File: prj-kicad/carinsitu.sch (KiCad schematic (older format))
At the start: 37 parts, among them P1 BAT, P2 MOT, P3 CONN_3, P4 CONN_1, SW1 SWITCH_SLIDE, U1 ESP32, U2 MIC2860, U3 STC3100, U4 SN74LVC1T45, U7 LSM6D3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

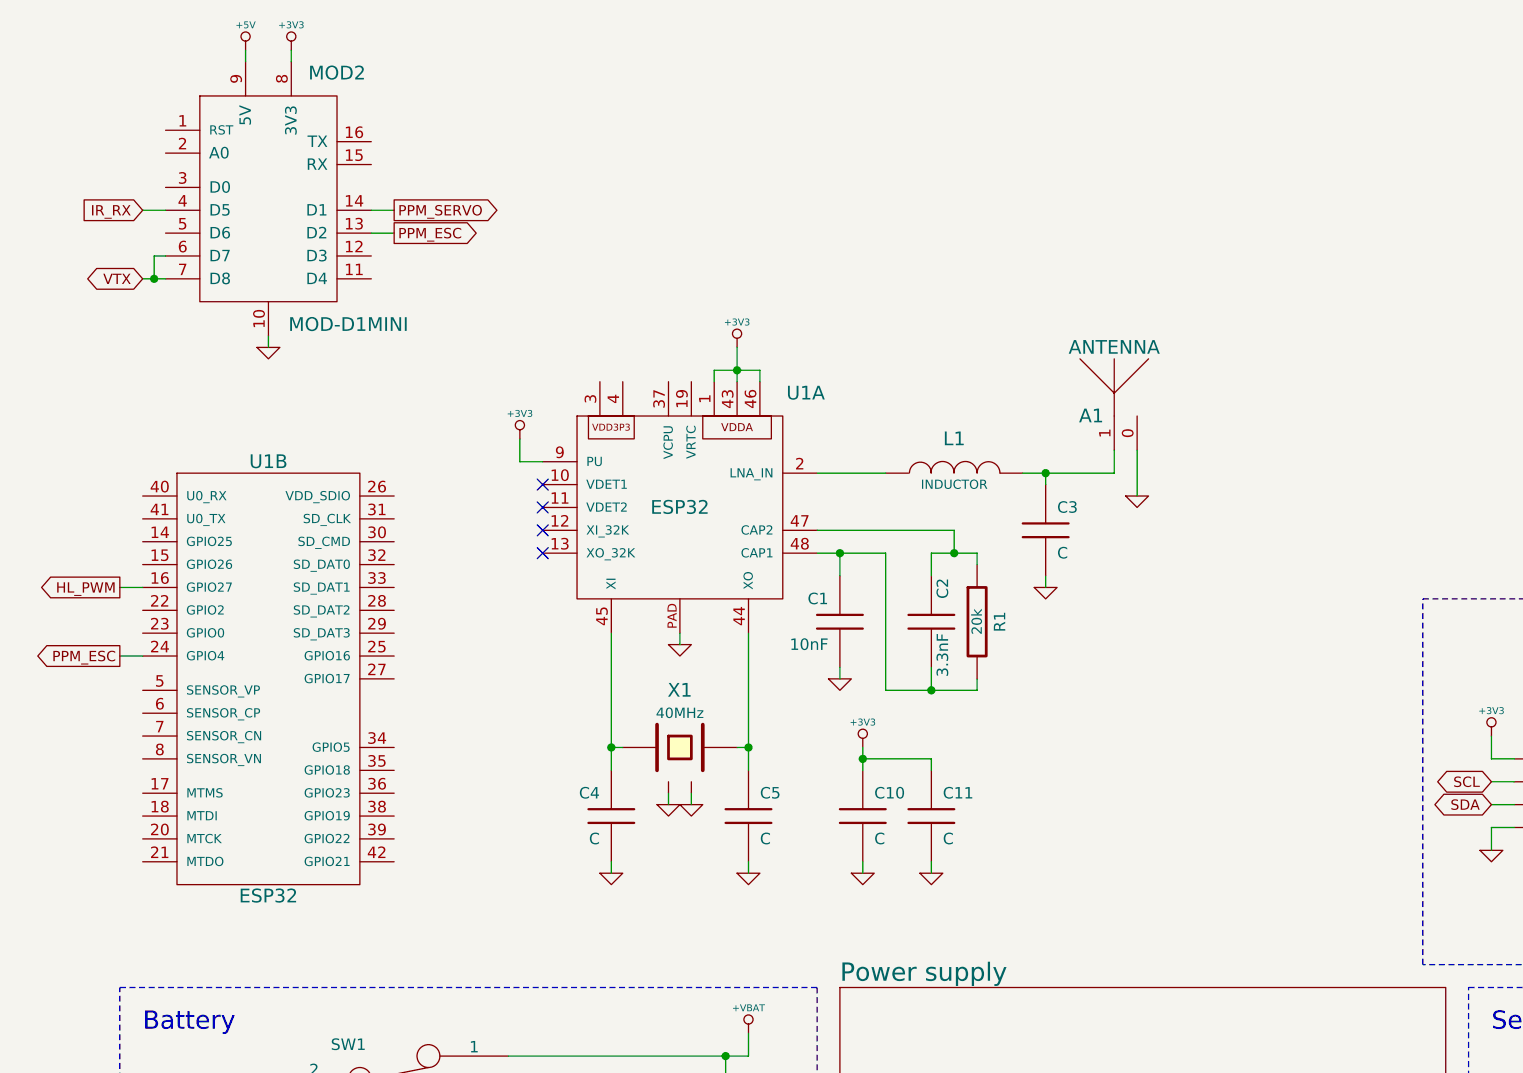
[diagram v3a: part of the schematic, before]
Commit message: = UPD: Replace ESP32 with ESP82xx to fit software requirements
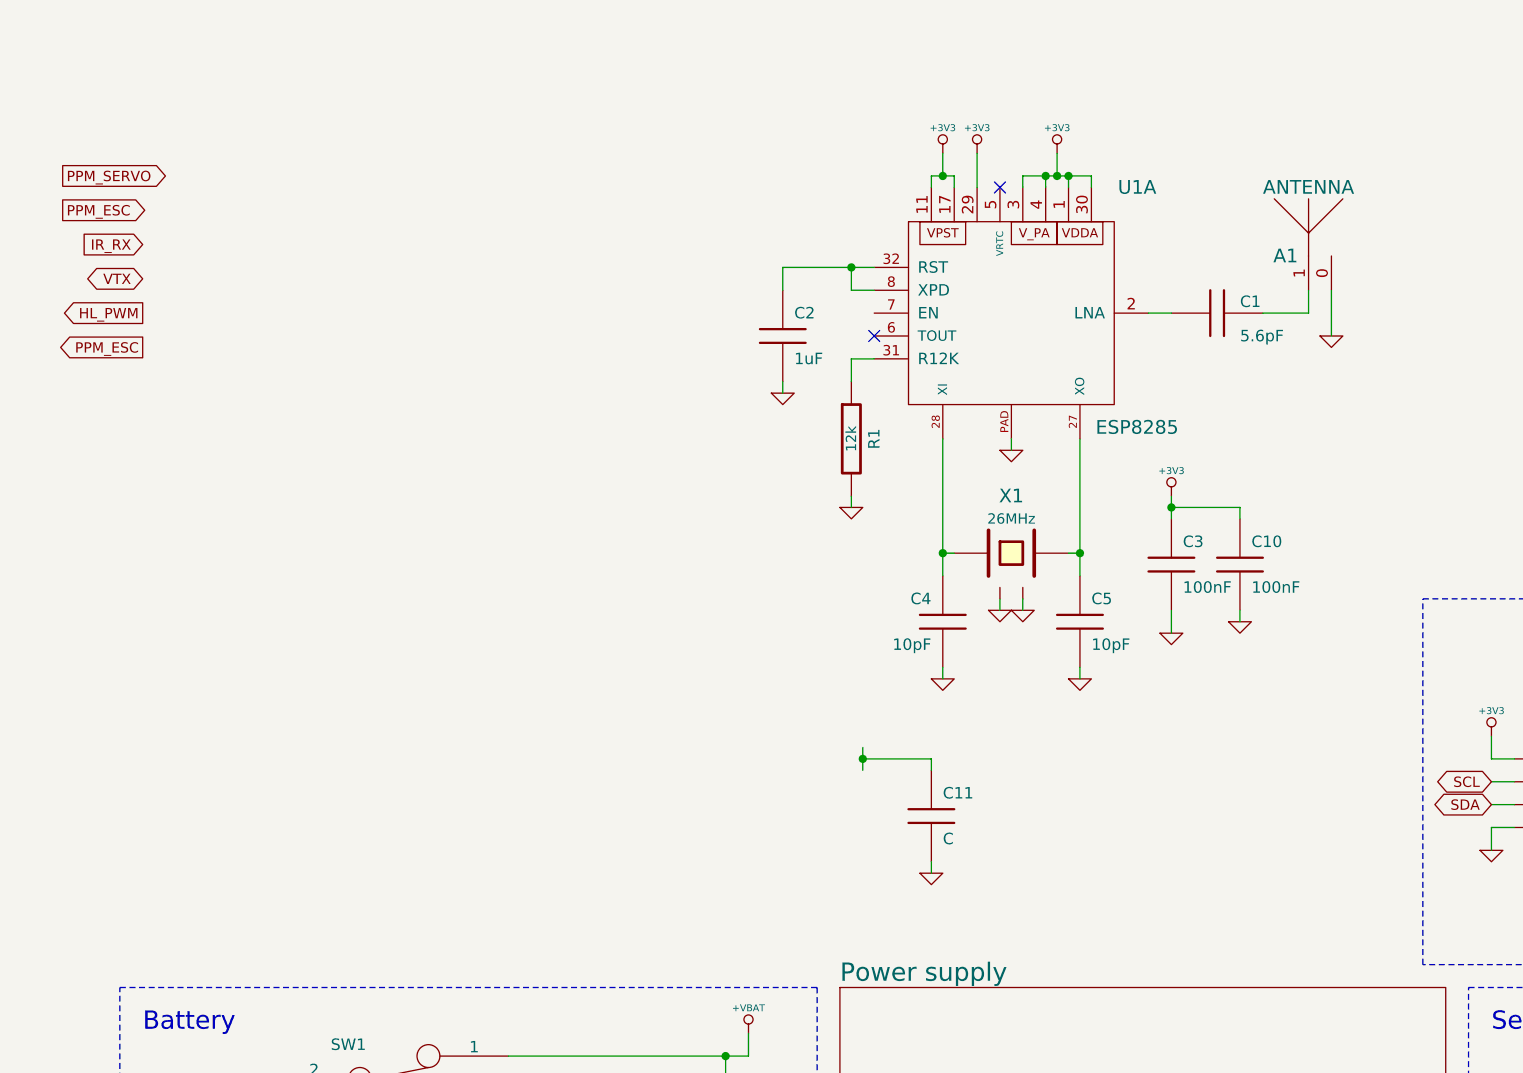
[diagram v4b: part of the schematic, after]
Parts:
- removed L1: INDUCTOR, carinsitu:SMD0603, symbol INDUCTOR
- removed MOD2: MOD-D1MINI, symbol MOD-D1MINI
- removed U1: ESP32, carinsitu:QFN48-04, symbol ESP32
- added U1: ESP8285, carinsitu:QFN32, symbol ESP8285
- C1: value 10nF -> 5.6pF
- C10, C3: value C -> 100nF
- C2: value 3.3nF -> 1uF
- C4, C5: value C -> 10pF
- R1: value 20k -> 12k
- X1: value 40MHz -> 26MHz; Manuf Ref (none) -> ABM8-26.000MHZ-10-1-U-T; Manufacturer (none) -> Abracon
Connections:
- net +3V3: now also C3.1, U1.1, U1.11, U1.17, U1.29, U1.3, U1.30, U1.4; no longer C11.1
- net GND: now also C2.2, R1.2, U1.PAD; no longer C1.2
- net at C5.1, X1.1: now also U1.27 (XO)
- net at C4.1, X1.3: now also U1.28 (XI)
- net at C2.1: now also U1.32 (RST), U1.8 (XPD); no longer R1.1
- net at A1.1: now also C1.1; no longer C3.1
- new net: C1.2, U1.2 (LNA)
- new net: R1.1, U1.31 (R12K)
- no-connect marks 9 -> 7
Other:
- moved on the sheet: A1, C1, C10, C2, C3, C4, C5, R1, X1

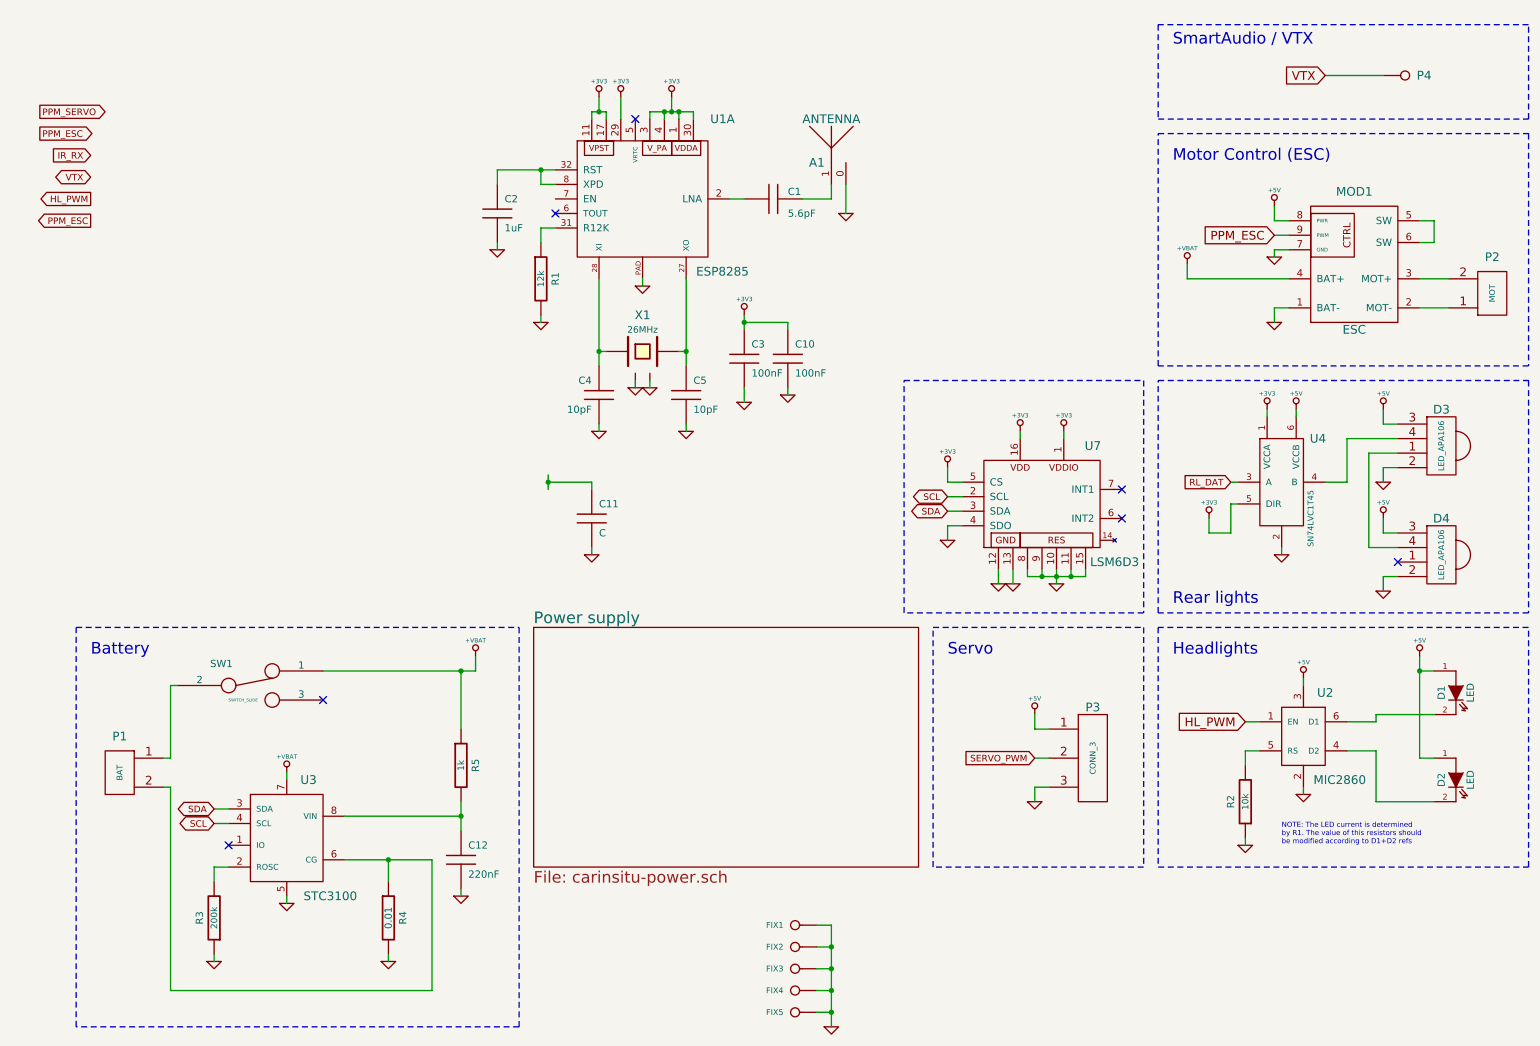
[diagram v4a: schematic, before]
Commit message: = UPD: Improve ESP82xx routing, connect main IOs (leds, esc, servo, ...)
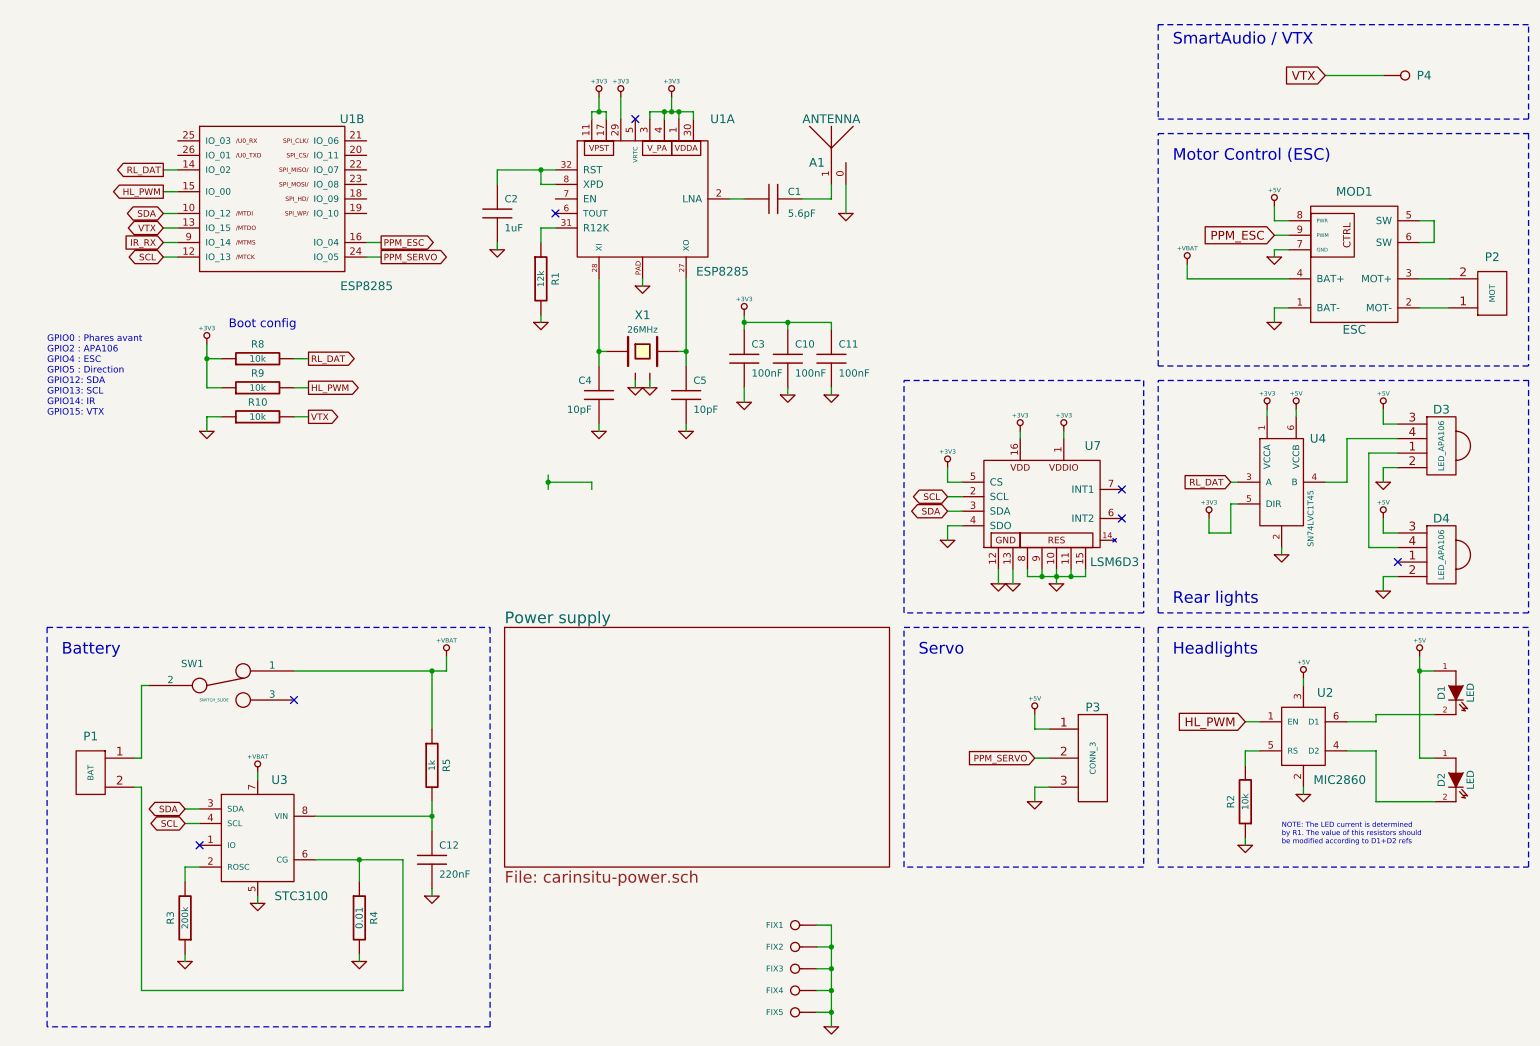
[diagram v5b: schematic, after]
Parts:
- added R10, R8, R9: 10k, carinsitu:SMD0603, symbol R
- added unit 2 of U1
- C11: value C -> 100nF
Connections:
- net SERVO_PWM is gone; now on net PPM_SERVO: P3.2 (P2)
- net +3V3: now also C11.1, R8.1, R9.1
- net GND: now also R10.1
- net HL_PWM: now also R9.2, U1.15 (IO_00)
- net IR_RX: now also U1.9 (IO_14)
- net PPM_ESC: now also U1.16 (IO_04)
- net PPM_SERVO: now also U1.24 (IO_05)
- net RL_DAT: now also R8.2, U1.14 (IO_02)
- net SCL: now also U1.12 (IO_13)
- net SDA: now also U1.10 (IO_12)
- net VTX: now also R10.2, U1.13 (IO_15)
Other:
- note added: "Boot config"
- note added: "GPIO0 : Phares avant\nGPIO2 : APA106\nGPIO4 : ESC\nGPIO5 : Direction\nGPIO12: SDA\nGPIO13: SCL\nGPIO14: IR\nGPIO15: VTX"
- moved on the sheet: C11, C12, P1, R3, R4, R5, SW1, U3

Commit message: = UPD: Replace battery gauge (STC3100 limited to 1 cell) by a MAX17205 ic
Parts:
- removed U3: STC3100, carinsitu:MSOP-8, symbol STC3100
- added C13, C14: C, carinsitu:SMD0603, symbol C
- added U3: MAX17205, carinsitu:TDFN14, symbol MAX17205
- C12: value 220nF -> 100nF
- R5: value 1k -> 50R
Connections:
- net GND: now also C13.2, C14.2, U3.13 (CELLX), U3.4 (CSN), U3.6 (CELL2), U3.7 (CELL1), U3.PAD
- net SCL: now also U3.11 (SCL)
- net SDA: now also U3.12 (SDA)
- net at P1.2 (PM), R4.1: now also U3.2 (CSP)
- net at R3.2: now also U3.9 (AIN1)
- net at C12.1, R5.2: now also U3.5 (VBAT)
- new net: C13.1, U3.1
- new net: C14.1, U3.3
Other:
- moved on the sheet: C12, R3, R4, R5

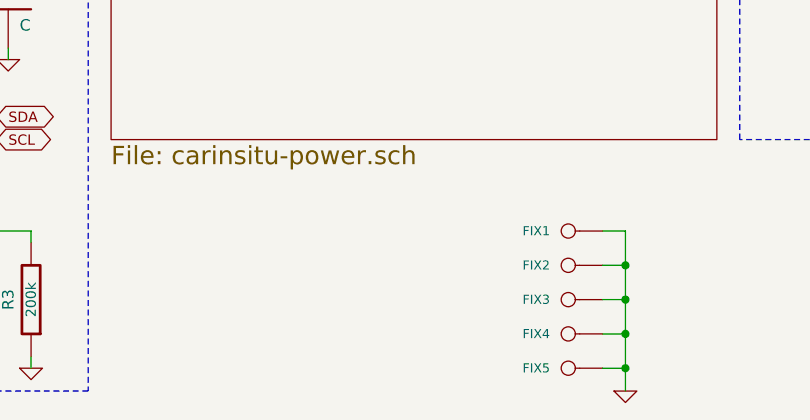
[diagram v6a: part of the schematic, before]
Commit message: = ADD: Insert test points for I2C and battery (2.54 grid)
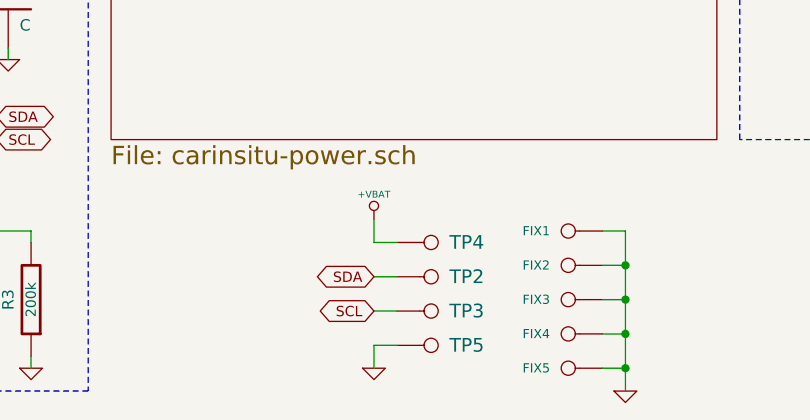
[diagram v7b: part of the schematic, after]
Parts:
- added TP2, TP3, TP4, TP5: CONN_1, carinsitu:TP, symbol CONN_1
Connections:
- net +VBAT: now also TP4.1
- net GND: now also TP5.1
- net SCL: now also TP3.1
- net SDA: now also TP2.1
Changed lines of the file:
@@
 Wire Wire Line
 	3300 6050 3300 6000
+$Comp
+L CONN_1 TP2
+U 1 1 5D26FA9E
+P 5450 7000
+F 0 "TP2" H 5530 7000 60  0000 L CNN
+F 1 "CONN_1" H 5450 7055 30  0001 C CNN
+F 2 "carinsitu:TP" H 5450 7000 60  0001 C CNN
+F 3 "" H 5450 7000 60  0000 C CNN
+	1    5450 7000
+	1    0    0    -1
+$EndComp
+$Comp
+L CONN_1 TP3
+U 1 1 5D26FC46
+P 5450 7150
+F 0 "TP3" H 5530 7150 60  0000 L CNN
+F 1 "CONN_1" H 5450 7205 30  0001 C CNN
+F 2 "carinsitu:TP" H 5450 7150 60  0001 C CNN
+F 3 "" H 5450 7150 60  0000 C CNN
+	1    5450 7150
+	1    0    0    -1
+$EndComp
+Text GLabel 5200 7000 0    45   BiDi ~ 0
+SDA
+Text GLabel 5200 7150 0    45   BiDi ~ 0
+SCL
+Wire Wire Line
+	5200 7150 5300 7150
+Wire Wire Line
+	5300 7000 5200 7000
+$Comp
+L CONN_1 TP4
+U 1 1 5D2702B4
+P 5450 6850
+F 0 "TP4" H 5530 6850 60  0000 L CNN
+F 1 "CONN_1" H 5450 6905 30  0001 C CNN
+F 2 "carinsitu:TP" H 5450 6850 60  0001 C CNN
+F 3 "" H 5450 6850 60  0000 C CNN
+	1    5450 6850
+	1    0    0    -1
+$EndComp
+$Comp
+L +VBAT #PWR053
+U 1 1 5D270442
+P 5200 6750
+F 0 "#PWR053" H 5200 6710 30  0001 C CNN
+F 1 "+VBAT" H 5200 6860 30  0000 C CNN
+F 2 "" H 5200 6750 60  0000 C CNN
+F 3 "" H 5200 6750 60  0000 C CNN
+	1    5200 6750
+	1    0    0    -1
+$EndComp
+Wire Wire Line
+	5200 6750 5200 6850
+Wire Wire Line
+	5200 6850 5300 6850
+$Comp
+L CONN_1 TP5
+U 1 1 5D2705FB
+P 5450 7300
+F 0 "TP5" H 5530 7300 60  0000 L CNN
+F 1 "CONN_1" H 5450 7355 30  0001 C CNN
+F 2 "carinsitu:TP" H 5450 7300 60  0001 C CNN
+F 3 "" H 5450 7300 60  0000 C CNN
+	1    5450 7300
+	1    0    0    -1
+$EndComp
+$Comp
+L GND #PWR054
+U 1 1 5D2706F6
+P 5200 7400
+F 0 "#PWR054" H 5200 7400 30  0001 C CNN
+F 1 "GND" H 5200 7330 30  0001 C CNN
+F 2 "" H 5200 7400 60  0000 C CNN
+F 3 "" H 5200 7400 60  0000 C CNN
+	1    5200 7400
+	1    0    0    -1
+$EndComp
+Wire Wire Line
+	5200 7400 5200 7300
+Wire Wire Line
+	5200 7300 5300 7300
 $EndSCHEMATC
